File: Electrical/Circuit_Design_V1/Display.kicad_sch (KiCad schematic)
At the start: 0 parts

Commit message: #3 Improving accelerometer schematic.
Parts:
- added C12: 1uF, symbol Device:C
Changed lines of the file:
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@@
 	(generator_version "9.0")
 	(paper "A4")
+	(symbol
+		(lib_id "Device:C")
+		(at 39.37 33.02 270)
+		(unit 1)
+		(exclude_from_sim no)
+		(in_bom yes)
+		(on_board yes)
+		(dnp no)
+		(property "Reference" "C12"
+			(at 36.322 30.988 90)
+			(effects
+				(font
+					(size 1.27 1.27)
+				)
+			)
+		)
+		(property "Value" "1uF"
+			(at 42.926 30.988 90)
+			(effects
+				(font
+					(size 1.27 1.27)
+				)
+			)
+		)
+		(property "Footprint" ""
+			(at 35.56 33.9852 0)
+			(effects
+				(font
+					(size 1.27 1.27)
+				)
+				(hide yes)
+			)
+		)
+		(property "Datasheet" "https://mm.digikey.com/Volume0/opasdata/d220001/medias/docus/6482/3372_0603B105K100XD.pdf"
+			(at 39.37 33.02 0)
+			(effects
+				(font
+					(size 1.27 1.27)
+				)
+				(hide yes)
+			)
+		)
+		(property "Description" "1 µF ±10% 10V Ceramic Capacitor X7R 0603 (1608 Metric)"
+			(at 39.37 33.02 0)
+			(effects
+				(font
+					(size 1.27 1.27)
+				)
+				(hide yes)
+			)
+		)
+		(property "Digikey Part Number" "3372-0603B105K100XDTR-ND"
+			(at 39.37 33.02 90)
+			(effects
+				(font
+					(size 1.27 1.27)
+				)
+				(hide yes)
+			)
+		)
+		(pin "1"
+		)
+		(pin "2"
+		)
+		(instances
+			(project "Circuit_Design_V1"
+				(path "/40e3562c-f358-42bb-8418-a7c96a575201/63e88297-887d-43ae-96c8-dfd9e2353300"
+					(reference "C12")
+					(unit 1)
+				)
+			)
+		)
+	)
 )

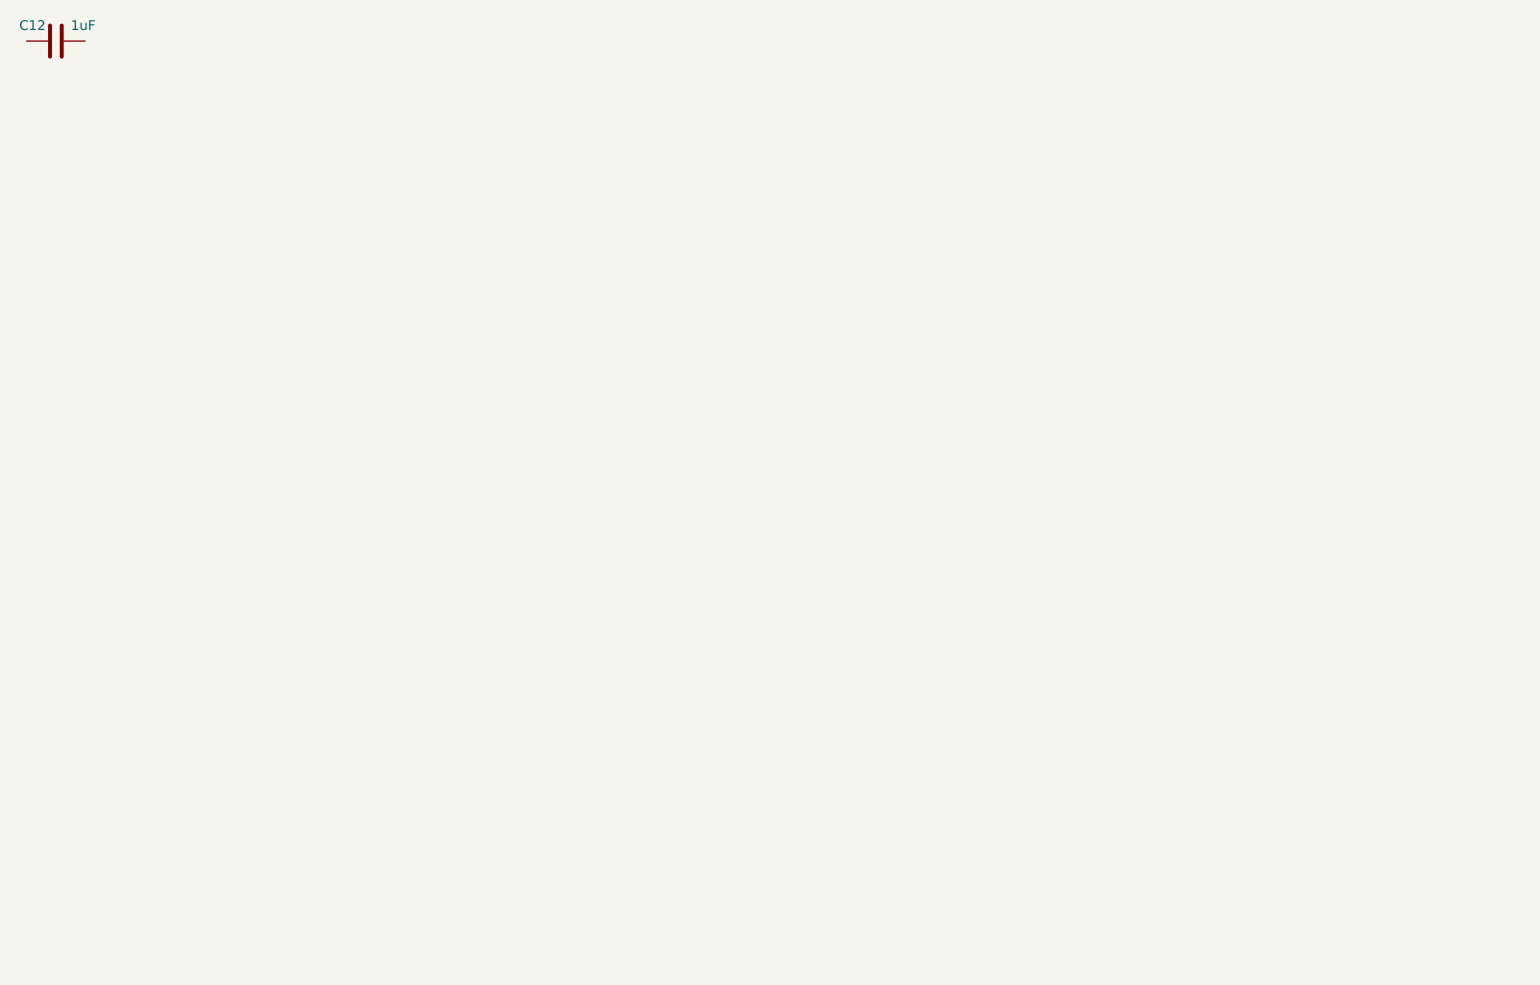
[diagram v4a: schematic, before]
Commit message: #3 Making symbols.
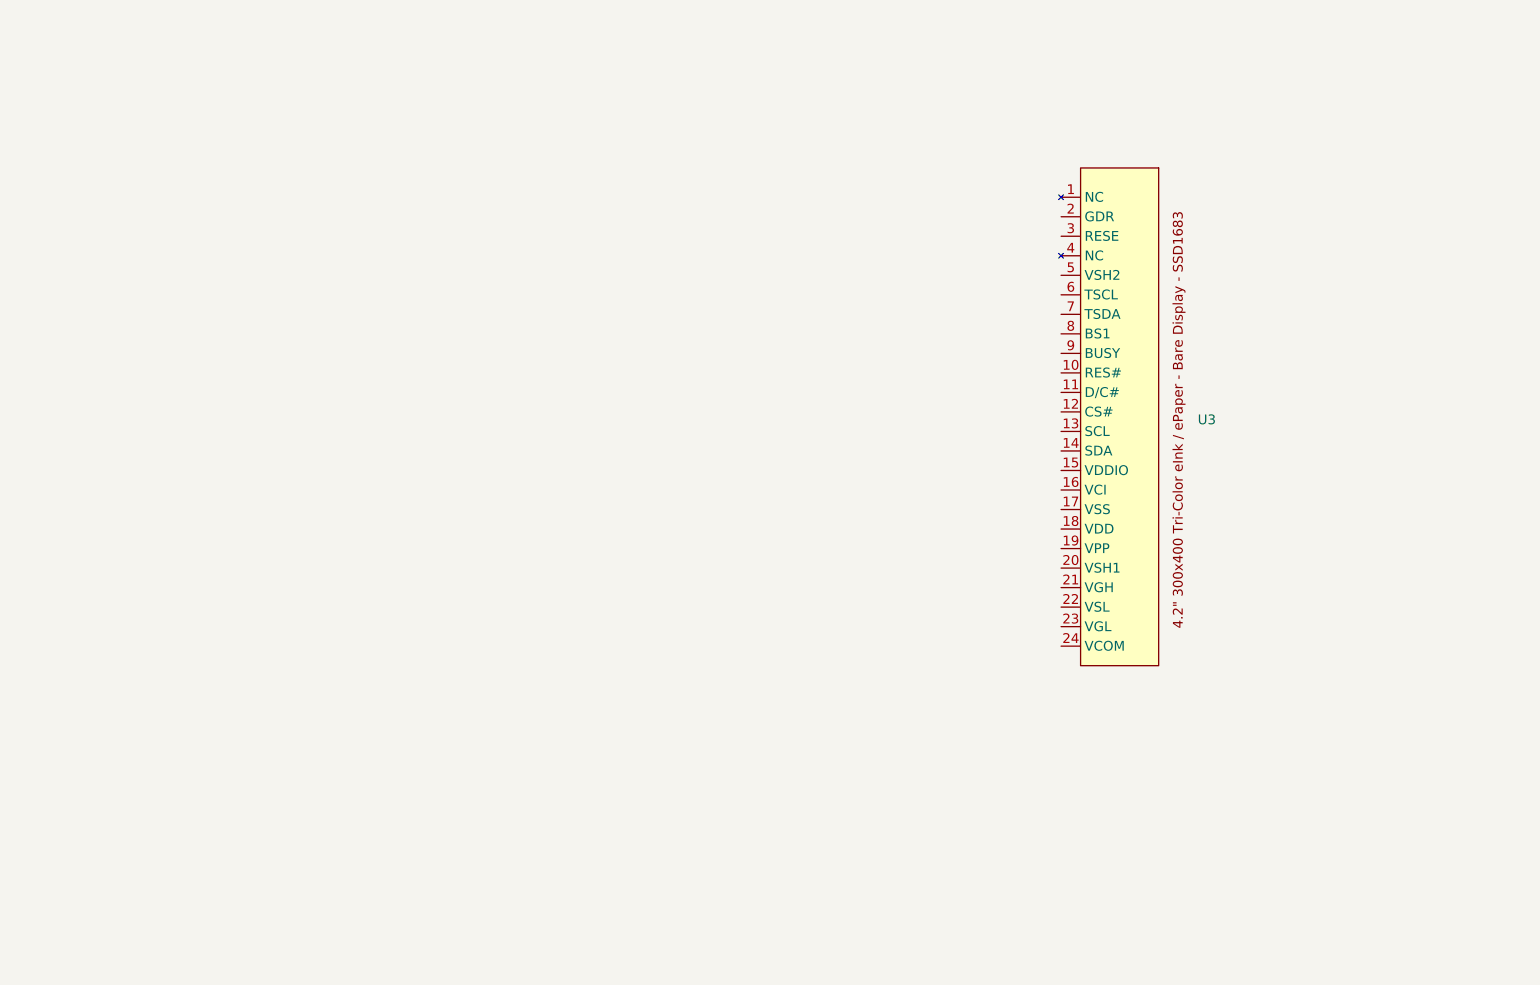
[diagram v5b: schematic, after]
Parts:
- removed C12: 1uF, symbol Device:C
- added U3: ~, symbol Etchasketch_hardware_symbol_library:4.2{dblquote}_300x400_Tri-Color_eInk_/_ePap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
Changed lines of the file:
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@@
 	(paper "A4")
 	(symbol
-		(lib_id "Device:C")
-		(at 39.37 33.02 270)
+		(lib_id "Etchasketch_hardware_symbol_library:4.2{dblquote}_300x400_Tri-Color_eInk_/_ePaper_-_Bare_Display_-_SSD1683")
+		(at 172.72 82.55 270)
 		(unit 1)
 		(exclude_from_sim no)
@@
 		(on_board yes)
 		(dnp no)
-		(property "Reference" "C12"
-			(at 36.322 30.988 90)
+		(fields_autoplaced yes)
+		(property "Reference" "U3"
+			(at 187.96 82.2959 90)
 			(effects
 				(font
 					(size 1.27 1.27)
 				)
+				(justify left)
 			)
 		)
-		(property "Value" "1uF"
-			(at 42.926 30.988 90)
-			(effects
-				(font
-					(size 1.27 1.27)
-				)
-			)
-		)
-		(property "Footprint" ""
-			(at 35.56 33.9852 0)
+		(property "Value" "~"
+			(at 172.72 82.55 0)
 			(effects
 				(font
@@
 			)
 		)
-		(property "Datasheet" "https://mm.digikey.com/Volume0/opasdata/d220001/medias/docus/6482/3372_0603B105K100XD.pdf"
-			(at 39.37 33.02 0)
+		(property "Footprint" ""
+			(at 172.72 82.55 0)
 			(effects
 				(font
@@
 			)
 		)
-		(property "Description" "1 µF ±10% 10V Ceramic Capacitor X7R 0603 (1608 Metric)"
-			(at 39.37 33.02 0)
+		(property "Datasheet" "https://cdn-shop.adafruit.com/product-files/6382/6382+C22266-001+datasheet+ZJY400300-042CABMFGN-R.pdf"
+			(at 172.72 82.55 0)
 			(effects
 				(font
@@
 			)
 		)
-		(property "Digikey Part Number" "3372-0603B105K100XDTR-ND"
-			(at 39.37 33.02 90)
+		(property "Description" "24-Pin FPC connector for E-Ink Display"
+			(at 172.72 82.55 0)
 			(effects
 				(font
@@
 			)
 		)
-		(pin "1"
+		(property "Digikey Part Number" "609-F33Z-1A7Q1-E8C24CT-ND"
+			(at 172.72 82.55 0)
+			(effects
+				(font
+					(size 1.27 1.27)
+				)
+				(hide yes)
+			)
+		)
+		(property "Adafruit Product ID" "6382"
+			(at 172.72 82.55 0)
+			(effects
+				(font
+					(size 1.27 1.27)
+				)
+				(hide yes)
+			)
+		)
+		(pin "5"
+		)
+		(pin "12"
+		)
+		(pin "14"
+		)
+		(pin "9"
+		)
+		(pin "19"
+		)
+		(pin "20"
+		)
+		(pin "21"
+		)
+		(pin "17"
+		)
+		(pin "22"
+		)
+		(pin "8"
+		)
+		(pin "15"
+		)
+		(pin "4"
+		)
+		(pin "10"
+		)
+		(pin "11"
+		)
+		(pin "3"
+		)
+		(pin "6"
+		)
+		(pin "7"
+		)
+		(pin "13"
+		)
+		(pin "16"
+		)
+		(pin "18"
+		)
+		(pin "23"
+		)
+		(pin "24"
 		)
 		(pin "2"
 		)
+		(pin "1"
+		)
 		(instances
-			(project "Circuit_Design_V1"
+			(project ""
 				(path "/40e3562c-f358-42bb-8418-a7c96a575201/63e88297-887d-43ae-96c8-dfd9e2353300"
-					(reference "C12")
+					(reference "U3")
 					(unit 1)
 				)

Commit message: #3 Finishing some circuitry.
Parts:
- added C12, C14, C15, C16, C17, C18, C19, C20, C21: 1uF, Capacitor_SMD:C_0805_2012Metric, symbol Device:C
- added D2, D3, D4: MBR0530, Diode_SMD:D_SOD-123, symbol Diode:MBR0530
- added L1: 47uH, Etchasketch_Footprints:Inductor, symbol Device:L
- added Q1: NMOS, Package_TO_SOT_SMD:TSOT-23, symbol Simulation_SPICE:NMOS
- added R3: 2.2Ω, Resistor_SMD:R_0805_2012Metric_Pad1.20x1.40mm_HandSolder, symbol Device:R
- added R4: 1650Ω, Resistor_SMD:R_0805_2012Metric, symbol Device:R
- added R5: 1370Ω, Resistor_SMD:R_0805_2012Metric, symbol Device:R
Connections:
- net +3.3V: now reaches U3.10 (RES#)
- net +3.3V: now also U3.15 (VDDIO), U3.16 (VCI), C17.2, R5.1
- net INK_D/C#: now reaches U3.11 (D/C#)
- net INK_CS#: now reaches U3.12 (CS#)
- net INK_SCL: now reaches U3.13 (SCL)
- net INK_SDA: now reaches U3.14 (SDA)
- net GND: now reaches U3.17 (VSS)
- net GND: now also U3.6 (TSCL), U3.7 (TSDA), U3.8 (BS1), C14.1, C15.1, C16.1, C17.1, C18.1, C19.1, C20.1, C21.1, D2.1 (K), R3.1, R4.1
- net at U3.18 (VDD): now also R4.2, R5.2
- net VPP: now reaches U3.19 (VPP)
- net GDR: now reaches U3.2 (GDR)
- net GDR: now also Q1.2 (G)
- net VSH1: now reaches U3.20 (VSH1)
- net VSH1: now also C18.2
- net VGH: now reaches U3.21 (VGH)
- net VGH: now also C15.2, C19.2, D4.1 (K)
- net VSL: now reaches U3.22 (VSL)
- net VSL: now also C20.2
- net VGL: now reaches U3.23 (VGL)
- net VGL: now also C14.2, D3.2 (A)
- net VCOM: now reaches U3.24 (VCOM)
- net VCOM: now also C21.2
- net RESE: now reaches U3.3 (RESE)
- net RESE: now also Q1.3 (S), R3.2
- net VSH2: now reaches U3.5 (VSH2)
- net VSH2: now also C16.2
- net INK_BUSY: now reaches U3.9 (BUSY)
- new net: C12.1, D2.2 (A), D3.1 (K)
- new net: C12.2, D4.2 (A), L1.1, Q1.1 (D)
- new net VCI: L1.2
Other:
- moved on the sheet: U3
